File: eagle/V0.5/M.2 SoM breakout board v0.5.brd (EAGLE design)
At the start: 140 x 122 mm, 136 parts, among them J1 3-PIN SMD, J11 WAFER-HY2.0-4PWB, J12 TP_OPEN, J13 SIM-NANO-4FF, J18 PARTICLE-STUDIOS_M_SERIES_M.2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, J19 TP_OPEN, J2 DCJ0202, J20 TP_OPEN, J21 SIP-2, J3 SPARK_CON_30X2_SMD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

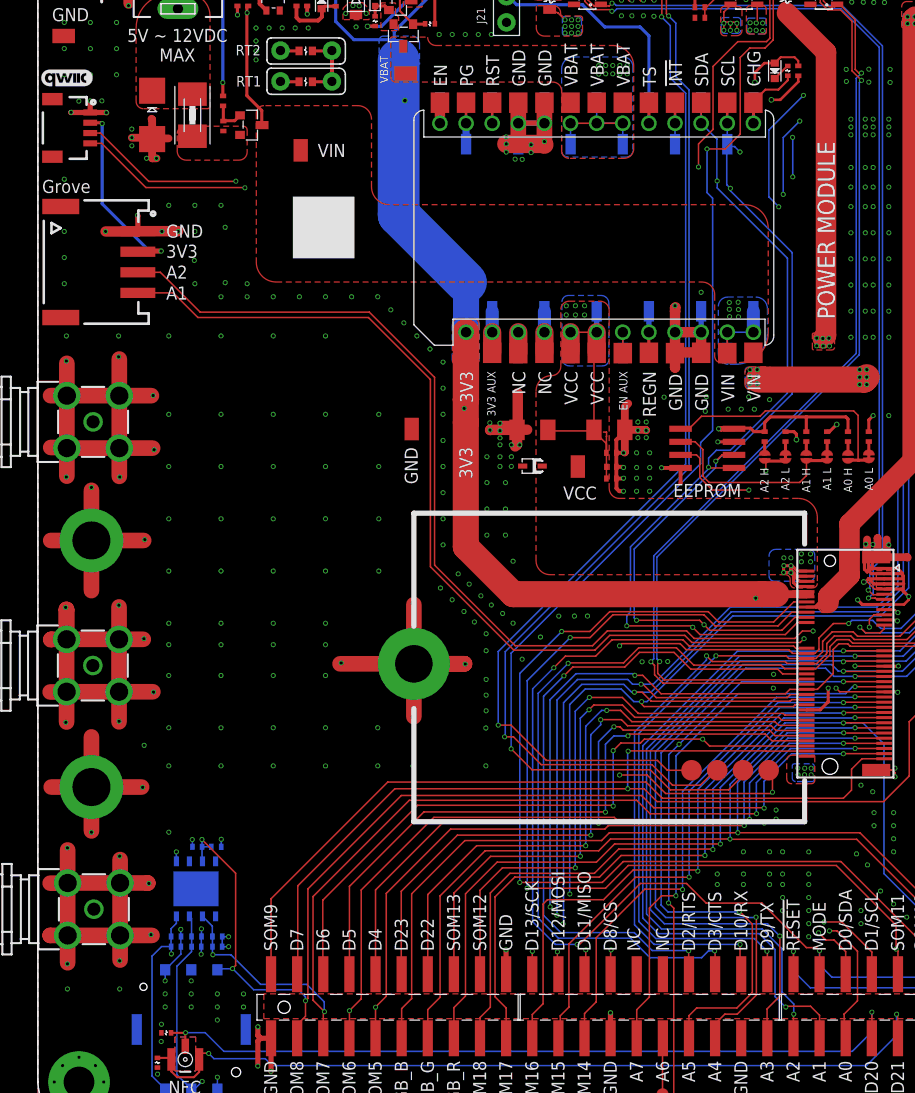
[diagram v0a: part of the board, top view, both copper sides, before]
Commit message: Added antenna cable clips
- added antenna cable clips
- moved qr code square to the bottom left
- moved VIN test point away from the clip to avoid accidental shorting
- added GND test point next to VIN test point
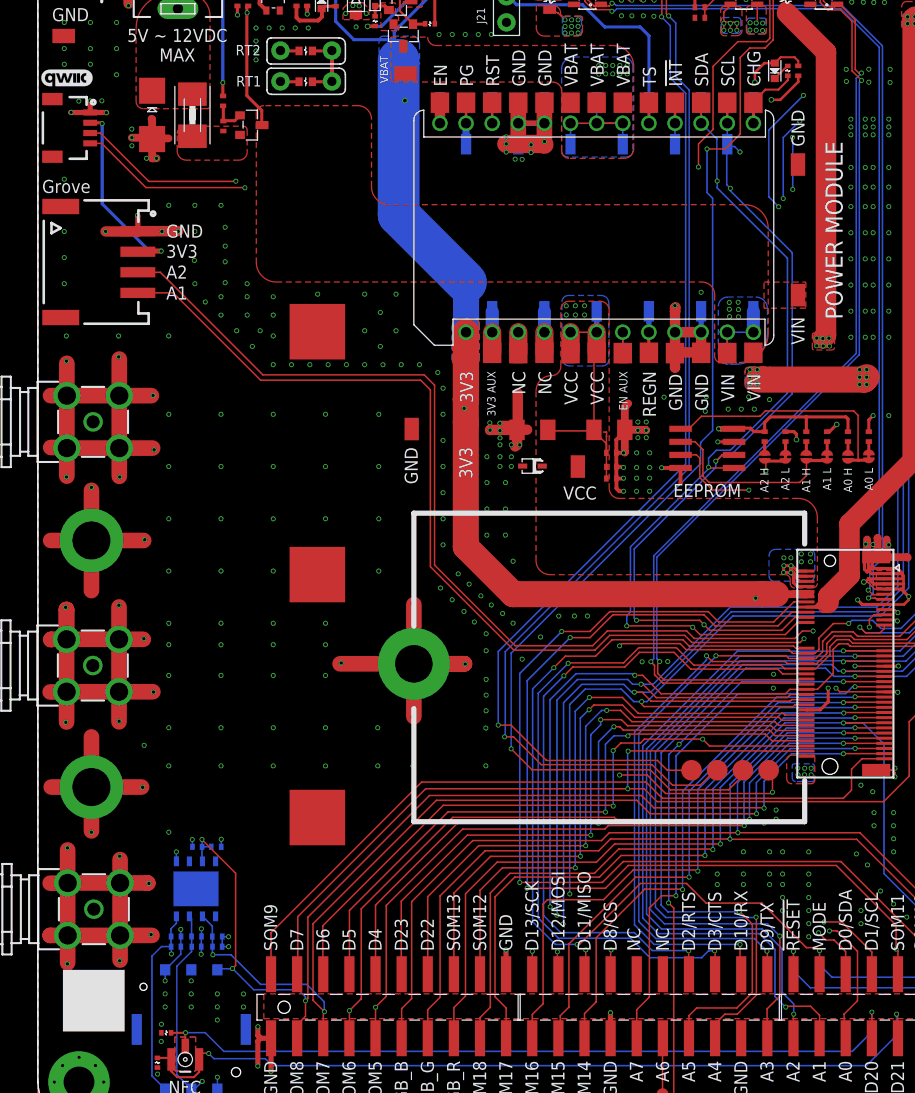
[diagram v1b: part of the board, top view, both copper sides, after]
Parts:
- added GND18: (no value), particle-studios:S2751-46R
- added X4, X5, X6: S8111-46R, particle-studios:S8111-46R
- moved VIN 50.4 mm to (73.9, 80.5)
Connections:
- net GND: now also GND18.1, X4.C, X5.C, X6.C
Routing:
- net SOM9: track 75.1 -> 73.2 mm
- net PWM3: track 196.4 -> 194.6 mm
- net SOM8: track 106.2 -> 104.6 mm
- net SOM7: track 111.5 -> 110.0 mm
- net PWM2: track 175.0 -> 173.5 mm
- net PWM1: track 184.5 -> 183.1 mm
- net PWM0: track 184.5 -> 183.4 mm
- net SOM6: track 111.7 -> 110.6 mm
- net SOM5: track 113.4 -> 112.7 mm
- net ADC1: track 213.8 -> 213.2 mm
- net GPIO1: track 123.7 -> 123.1 mm
- net !RESET: track 277.3 -> 276.8 mm
- net GND: vias 759 -> 773

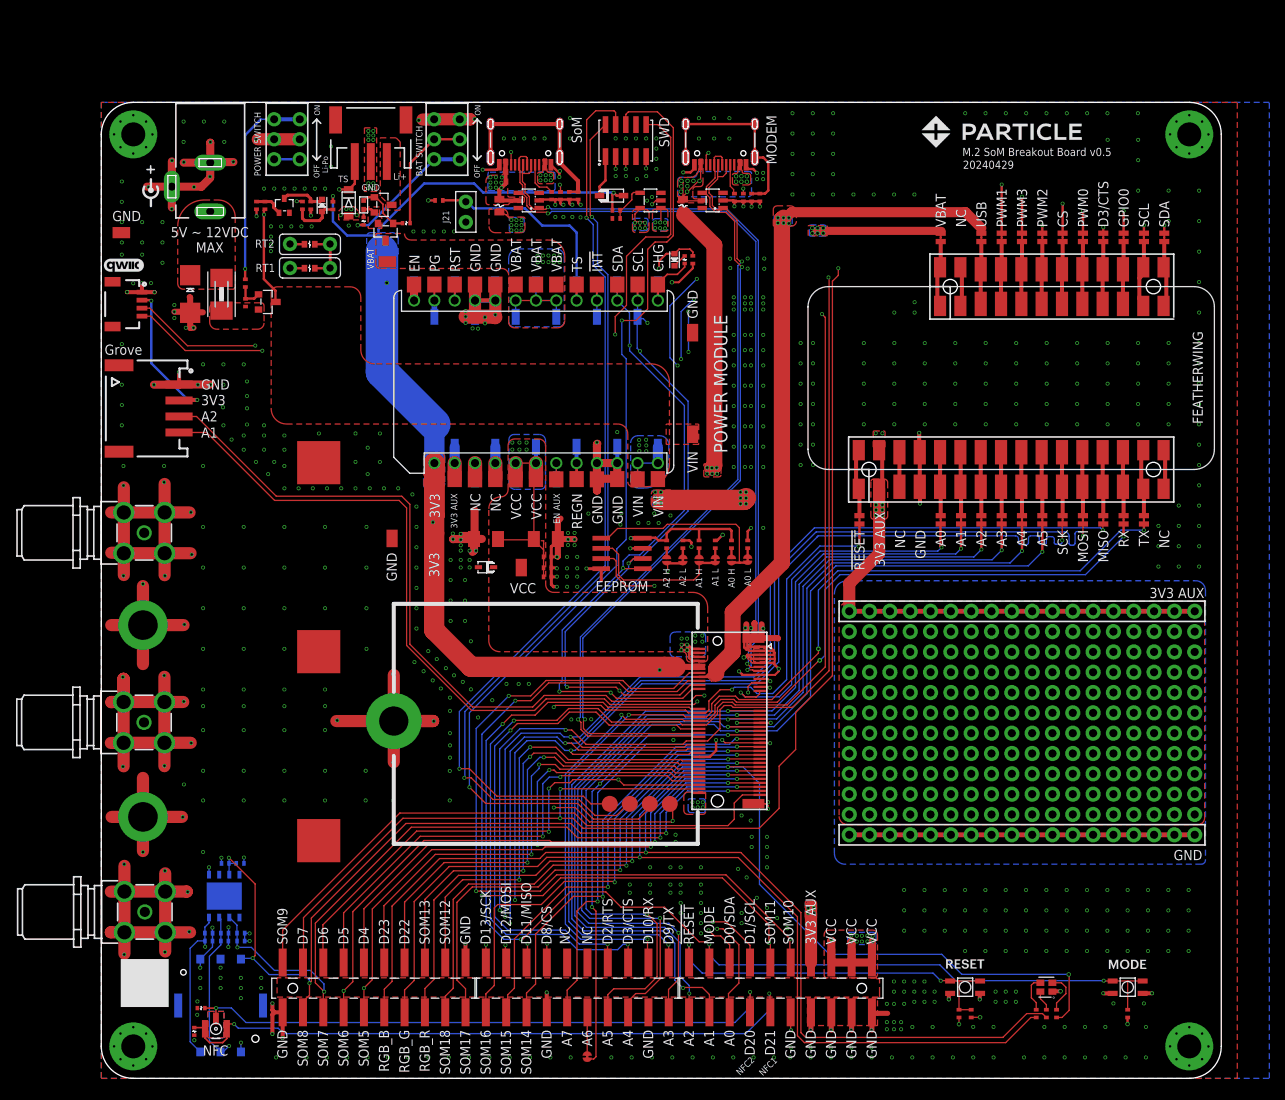
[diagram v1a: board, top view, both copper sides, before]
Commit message: update
1.Check the DRC again and remove the GND via short circuit bug
2.Modify the package and test point offset issue
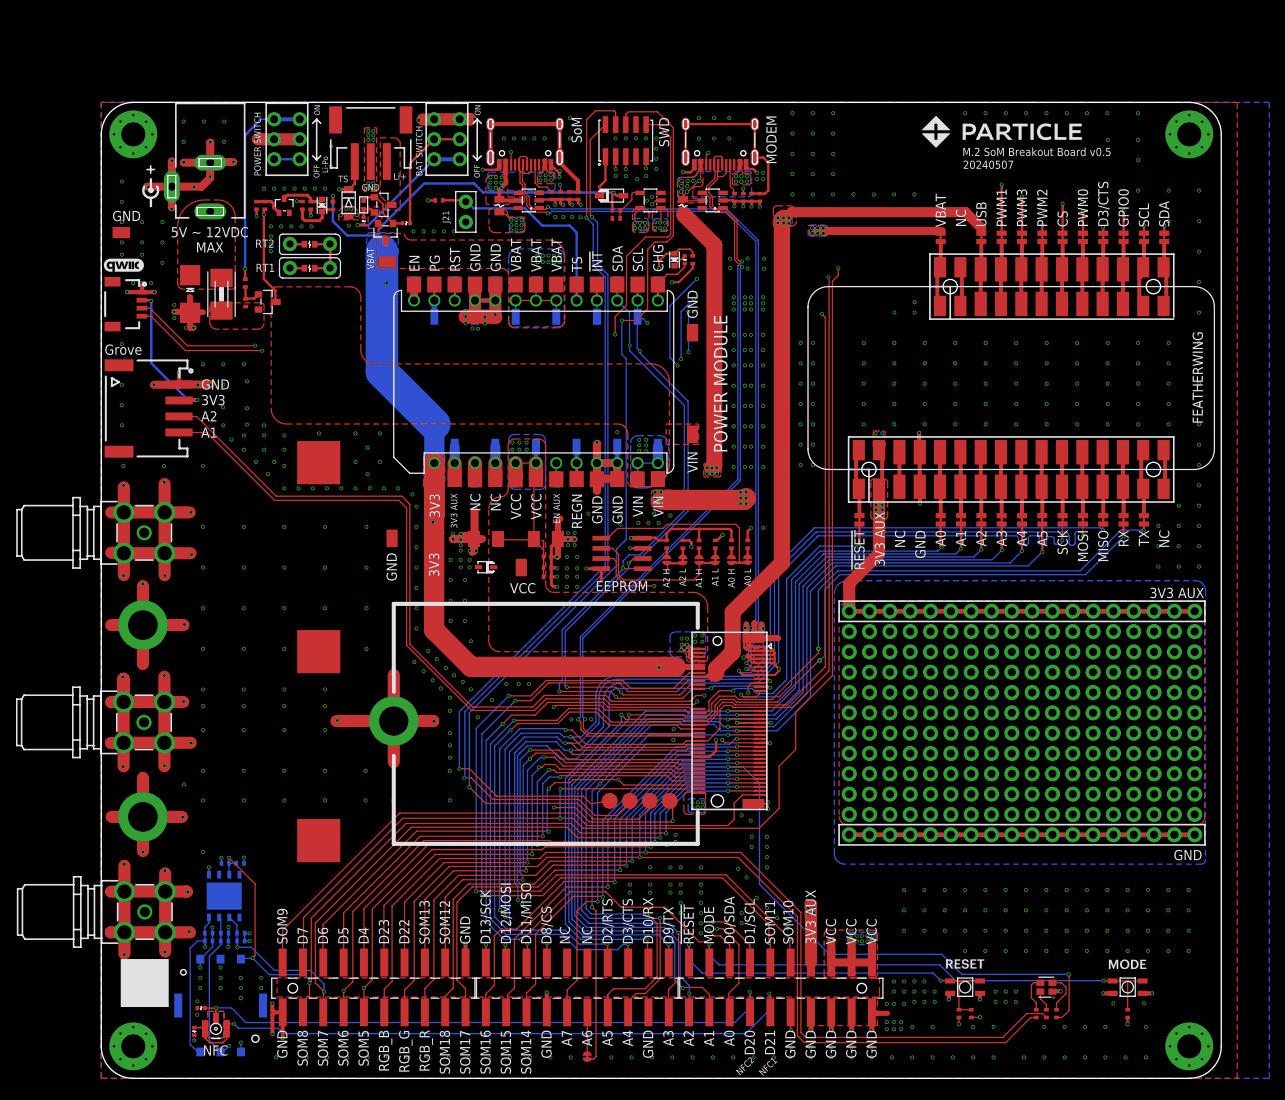
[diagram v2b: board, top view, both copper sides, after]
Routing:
- net GND: track 608.2 -> 673.7 mm, vias 773 -> 774
- net SCK: track 138.8 -> 141.1 mm
- net SOM16: track 59.3 -> 57.3 mm
- net MOSI: track 138.8 -> 140.8 mm
- net MISO: track 139.2 -> 141.1 mm
- net ADC0: track 90.8 -> 90.2 mm
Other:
- board text added: "20240507"
- board text removed: "20240429"

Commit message: update
update
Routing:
- net GND: track 673.7 -> 708.0 mm
- net SWCLK: track 116.6 -> 116.0 mm
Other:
- board text added: "G3"
- board text added: "L1"
- board text added: "L4"
- board text added: "P2"
